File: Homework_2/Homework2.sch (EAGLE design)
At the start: 22 parts

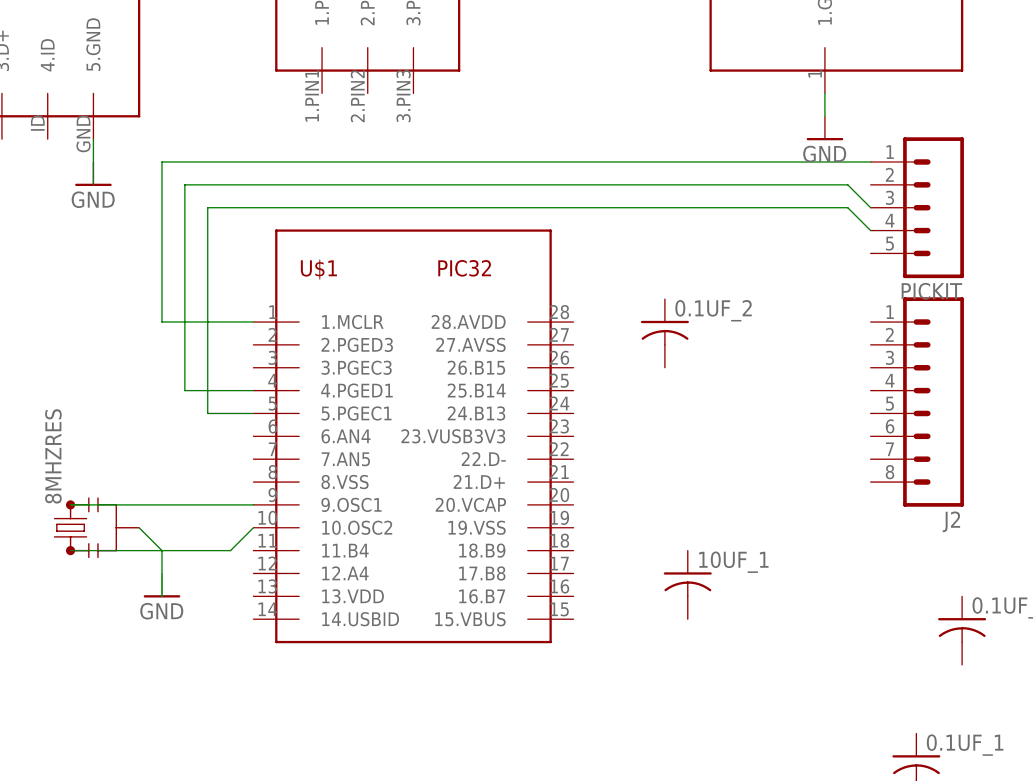
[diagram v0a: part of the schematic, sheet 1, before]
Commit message: Homework2/3_commit4
more schematic work
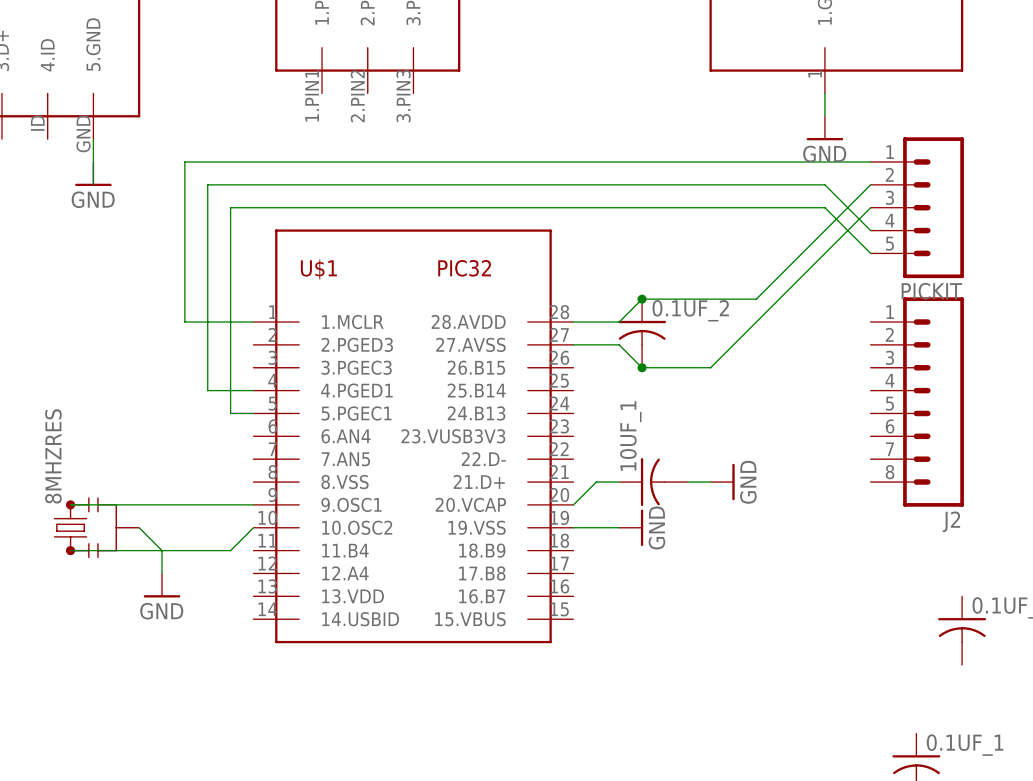
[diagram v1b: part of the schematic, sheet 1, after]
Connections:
- removed net N$3: 8MHZRES.2
- new net N$10: 10UF_1.1, U$1.20.VCAP
- new net N$8: 0.1UF_2.2, PICKIT.3, U$1.27.AVSS
- new net N$9: 0.1UF_2.1, PICKIT.2, U$1.28.AVDD
- net GND: now also 10UF_1.2, 8MHZRES.2, U$1.19.VSS
- net N$6: now also PICKIT.4; no longer PICKIT.3
- net N$7: now also PICKIT.5; no longer PICKIT.4
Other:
- moved on the sheet: 0.1UF_2, 10UF_1
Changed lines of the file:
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@@
 <part name="GND2" library="Homework2" deviceset="GND" device=""/>
 <part name="GND3" library="Homework2" deviceset="GND" device=""/>
+<part name="GND4" library="Homework2" deviceset="GND" device=""/>
+<part name="GND5" library="Homework2" deviceset="GND" device=""/>
 </parts>
 <sheets>
@@
 <instance part="PICKIT" gate="G$1" x="134.62" y="73.66" rot="R180"/>
 <instance part="U$3" gate="G$1" x="30.48" y="88.9" rot="R90"/>
-<instance part="10UF_1" gate="G$1" x="106.68" y="33.02"/>
+<instance part="10UF_1" gate="G$1" x="101.6" y="43.18" rot="R90"/>
 <instance part="0.1UF_4" gate="G$1" x="152.4" y="12.7"/>
 <instance part="0.1UF_1" gate="G$1" x="132.08" y="12.7"/>
-<instance part="0.1UF_2" gate="G$1" x="104.14" y="60.96"/>
+<instance part="0.1UF_2" gate="G$1" x="101.6" y="60.96"/>
 <instance part="0.1UF_3" gate="G$1" x="137.16" y="27.94"/>
 <instance part="330_R1" gate="G$1" x="40.64" y="-5.08"/>
@@
 <instance part="GND2" gate="1" x="40.64" y="76.2"/>
 <instance part="GND3" gate="1" x="121.92" y="81.28"/>
+<instance part="GND4" gate="1" x="101.6" y="38.1" rot="R90"/>
+<instance part="GND5" gate="1" x="111.76" y="43.18" rot="R90"/>
 </instances>
 <busses>
@@
 </segment>
 </net>
-<net name="N$3" class="0">
-<segment>
-<pinref part="8MHZRES" gate="G$1" pin="2"/>
-<wire x1="45.72" y1="38.1" x2="48.26" y2="35.56" width="0.1524" layer="91"/>
-<wire x1="48.26" y1="35.56" x2="48.26" y2="30.48" width="0.1524" layer="91"/>
-</segment>
-</net>
 <net name="GND" class="0">
 <segment>
@@
 <pinref part="GND3" gate="1" pin="GND"/>
 <wire x1="121.92" y1="86.36" x2="121.92" y2="83.82" width="0.1524" layer="91"/>
+</segment>
+<segment>
+<pinref part="U$1" gate="G$1" pin="19.VSS"/>
+<pinref part="GND4" gate="1" pin="GND"/>
+<wire x1="93.98" y1="38.1" x2="99.06" y2="38.1" width="0.1524" layer="91"/>
+</segment>
+<segment>
+<pinref part="10UF_1" gate="G$1" pin="2"/>
+<pinref part="GND5" gate="1" pin="GND"/>
+<wire x1="106.68" y1="43.18" x2="109.22" y2="43.18" width="0.1524" layer="91"/>
+</segment>
+<segment>
+<pinref part="8MHZRES" gate="G$1" pin="2"/>
+<pinref part="GND1" gate="1" pin="GND"/>
+<wire x1="45.72" y1="38.1" x2="48.26" y2="35.56" width="0.1524" layer="91"/>
+<wire x1="48.26" y1="35.56" x2="48.26" y2="33.02" width="0.1524" layer="91"/>
 </segment>
 </net>
@@
 <segment>
 <pinref part="PICKIT" gate="G$1" pin="1"/>
-<wire x1="48.26" y1="78.74" x2="127" y2="78.74" width="0.1524" layer="91"/>
-<wire x1="48.26" y1="78.74" x2="48.26" y2="60.96" width="0.1524" layer="91"/>
+<wire x1="50.8" y1="78.74" x2="127" y2="78.74" width="0.1524" layer="91"/>
+<wire x1="50.8" y1="78.74" x2="50.8" y2="60.96" width="0.1524" layer="91"/>
 <pinref part="U$1" gate="G$1" pin="1.MCLR"/>
-<wire x1="58.42" y1="60.96" x2="48.26" y2="60.96" width="0.1524" layer="91"/>
+<wire x1="58.42" y1="60.96" x2="50.8" y2="60.96" width="0.1524" layer="91"/>
+</segment>
+</net>
+<net name="N$8" class="0">
+<segment>
+<pinref part="0.1UF_2" gate="G$1" pin="2"/>
+<pinref part="U$1" gate="G$1" pin="27.AVSS"/>
+<wire x1="101.6" y1="55.88" x2="99.06" y2="58.42" width="0.1524" layer="91"/>
+<wire x1="99.06" y1="58.42" x2="93.98" y2="58.42" width="0.1524" layer="91"/>
+<pinref part="PICKIT" gate="G$1" pin="3"/>
+<wire x1="127" y1="73.66" x2="109.22" y2="55.88" width="0.1524" layer="91"/>
+<wire x1="109.22" y1="55.88" x2="101.6" y2="55.88" width="0.1524" layer="91"/>
+<junction x="101.6" y="55.88"/>
+</segment>
+</net>
+<net name="N$9" class="0">
+<segment>
+<pinref part="0.1UF_2" gate="G$1" pin="1"/>
+<pinref part="U$1" gate="G$1" pin="28.AVDD"/>
+<wire x1="101.6" y1="63.5" x2="99.06" y2="60.96" width="0.1524" layer="91"/>
+<wire x1="99.06" y1="60.96" x2="93.98" y2="60.96" width="0.1524" layer="91"/>
+<pinref part="PICKIT" gate="G$1" pin="2"/>
+<wire x1="127" y1="76.2" x2="114.3" y2="63.5" width="0.1524" layer="91"/>
+<wire x1="114.3" y1="63.5" x2="101.6" y2="63.5" width="0.1524" layer="91"/>
+<junction x="101.6" y="63.5"/>
 </segment>
 </net>
 <net name="N$6" class="0">
 <segment>
-<pinref part="PICKIT" gate="G$1" pin="3"/>
-<wire x1="127" y1="73.66" x2="124.46" y2="76.2" width="0.1524" layer="91"/>
-<wire x1="124.46" y1="76.2" x2="50.8" y2="76.2" width="0.1524" layer="91"/>
-<wire x1="50.8" y1="76.2" x2="50.8" y2="53.34" width="0.1524" layer="91"/>
+<pinref part="PICKIT" gate="G$1" pin="4"/>
+<wire x1="127" y1="71.12" x2="121.92" y2="76.2" width="0.1524" layer="91"/>
+<wire x1="121.92" y1="76.2" x2="53.34" y2="76.2" width="0.1524" layer="91"/>
+<wire x1="53.34" y1="76.2" x2="53.34" y2="53.34" width="0.1524" layer="91"/>
 <pinref part="U$1" gate="G$1" pin="4.PGED1"/>
-<wire x1="50.8" y1="53.34" x2="58.42" y2="53.34" width="0.1524" layer="91"/>
+<wire x1="53.34" y1="53.34" x2="58.42" y2="53.34" width="0.1524" layer="91"/>
 </segment>
 </net>
 <net name="N$7" class="0">
 <segment>
-<pinref part="PICKIT" gate="G$1" pin="4"/>
-<wire x1="127" y1="71.12" x2="124.46" y2="73.66" width="0.1524" layer="91"/>
-<wire x1="124.46" y1="73.66" x2="53.34" y2="73.66" width="0.1524" layer="91"/>
-<wire x1="53.34" y1="73.66" x2="53.34" y2="50.8" width="0.1524" layer="91"/>
+<pinref part="PICKIT" gate="G$1" pin="5"/>
+<wire x1="127" y1="68.58" x2="121.92" y2="73.66" width="0.1524" layer="91"/>
+<wire x1="121.92" y1="73.66" x2="55.88" y2="73.66" width="0.1524" layer="91"/>
+<wire x1="55.88" y1="73.66" x2="55.88" y2="50.8" width="0.1524" layer="91"/>
 <pinref part="U$1" gate="G$1" pin="5.PGEC1"/>
-<wire x1="53.34" y1="50.8" x2="58.42" y2="50.8" width="0.1524" layer="91"/>
+<wire x1="55.88" y1="50.8" x2="58.42" y2="50.8" width="0.1524" layer="91"/>
 </segment>
 </net>
+<net name="N$10" class="0">
+<segment>
+<pinref part="U$1" gate="G$1" pin="20.VCAP"/>
+<pinref part="10UF_1" gate="G$1" pin="1"/>
+<wire x1="93.98" y1="40.64" x2="96.52" y2="43.18" width="0.1524" layer="91"/>
+<wire x1="96.52" y1="43.18" x2="99.06" y2="43.18" width="0.1524" layer="91"/>
+</segment>
+</net>

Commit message: Homework_2/3_commit#5
finished schematic
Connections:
- net N$6 renamed PGED1
- net N$7 renamed PGEC1
- removed net N$4: U$3.5.GND
- removed net N$5: PICKIT.1, U$1.1.MCLR
- new net +3V3: 10K_R3.2, 10K_R4.1
- new net A0: J2.8, U$1.2.PGED3
- new net A1: J2.7, U$1.3.PGEC3
- new net A4: GREEN_LED.A, J2.3, U$1.12.A4
- new net B13: J1.6, U$1.24.B13
- new net B14: J1.7, U$1.25.B14
- new net B15: J1.8, U$1.26.B15
- new net B2: J2.6, U$1.6.AN4
- new net B3: J2.5, U$1.7.AN5
- new net B4: 10K_R4.2, J2.4, U$1.11.B4, USER.3
- new net B7: J1.3, U$1.16.B7
- new net B8: J1.4, U$1.17.B8
- new net B9: J1.5, U$1.18.B9
- new net D+: U$1.21.D+, U$3.3.D+
- new net D-: U$1.22.D-, U$3.2.D-
- new net MCLR: 10K_R3.1, PICKIT.1, RESET.3, U$1.1.MCLR
- new net N$3: 330_R1.1
- new net OSC1: 8MHZRES.1, U$1.9.OSC1
- new net OSC2: 8MHZRES.3, U$1.10.OSC2
- new net USBID: U$1.14.USBID, U$3.4.ID
- new net VBUS+5: 0.1UF_1.1, J1.2, U$1.15.VBUS, U$2.2.VIN, U$3.1.VBUS, U$4.2.PIN2, U$4.3.PIN3
- new net VDD: 0.1UF_3.1, 0.1UF_4.2, 10UF_2.1, J2.2, RED_LED.A, U$1.13.VDD, U$2.3.VOUT
- net GND: now also 0.1UF_1.2, 0.1UF_3.2, 0.1UF_4.1, 10UF_2.2, 330_R2.1, J1.1, J2.1, RESET.1, U$1.8.VSS, U$3.5.GND, USER.1
- net N$1: now also 330_R2.2, GREEN_LED.C; no longer 8MHZRES.3, U$1.9.OSC1
- net N$2: now also 330_R1.2, RED_LED.C; no longer 8MHZRES.1, U$1.10.OSC2
- net N$9: now also U$1.23.VUSB3V3
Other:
- moved on the sheet: 0.1UF_1, 0.1UF_2, 0.1UF_3, 0.1UF_4, 10K_R3, 10K_R4, 10UF_1, 10UF_2, 330_R1, 330_R2, 8MHZRES, GREEN_LED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

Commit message: homework_2/3_commit#6
brd before error checking
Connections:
- removed net N$3: 330_R1.1
- net GND: now also 330_R1.1
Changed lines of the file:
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@@
 <wire x1="48.26" y1="10.16" x2="48.26" y2="7.62" width="0.1524" layer="91"/>
+</segment>
+<segment>
+<pinref part="330_R1" gate="G$1" pin="1"/>
+<wire x1="-17.78" y1="17.78" x2="-17.78" y2="15.24" width="0.1524" layer="91"/>
+<label x="-17.78" y="10.16" size="1.778" layer="95"/>
 </segment>
 </net>
@@
 </segment>
 </net>
-<net name="N$3" class="0">
-<segment>
-<pinref part="330_R1" gate="G$1" pin="1"/>
-<wire x1="-17.78" y1="17.78" x2="-17.78" y2="15.24" width="0.1524" layer="91"/>
-<label x="-17.78" y="10.16" size="1.778" layer="95"/>
-</segment>
-</net>

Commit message: board files
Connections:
- removed net N$8: 0.1UF_2.2, PICKIT.3, U$1.27.AVSS
- net GND: now also 0.1UF_2.2, PICKIT.3, U$1.27.AVSS
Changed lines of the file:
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@@
 <part name="GND1" library="Homework2" deviceset="GND" device=""/>
 <part name="GND2" library="Homework2" deviceset="GND" device=""/>
+<part name="GND3" library="Homework2" deviceset="GND" device=""/>
 </parts>
 <sheets>
@@
 <instance part="GND1" gate="1" x="142.24" y="124.46" rot="R180"/>
 <instance part="GND2" gate="1" x="48.26" y="5.08"/>
+<instance part="GND3" gate="1" x="93.98" y="73.66" rot="R180"/>
 </instances>
 <busses>
@@
 <label x="-17.78" y="10.16" size="1.778" layer="95"/>
 </segment>
-</net>
-<net name="N$8" class="0">
 <segment>
 <pinref part="0.1UF_2" gate="G$1" pin="2"/>
@@
 <wire x1="109.22" y1="58.42" x2="101.6" y2="58.42" width="0.1524" layer="91"/>
 <junction x="101.6" y="58.42"/>
+<wire x1="93.98" y1="58.42" x2="93.98" y2="71.12" width="0.1524" layer="91"/>
+<junction x="93.98" y="58.42"/>
+<pinref part="GND3" gate="1" pin="GND"/>
 </segment>
 </net>
